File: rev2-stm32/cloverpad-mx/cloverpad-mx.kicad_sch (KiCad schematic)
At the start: 31 parts, among them J1 USB_C_Receptacle_USB2.0_16P, J2 Conn_01x04, SW1 SW_SPST, SW2 SW_SPST, U1 STM32F072CBT6, U2 XC6206PxxxMR, Y1 16MHz

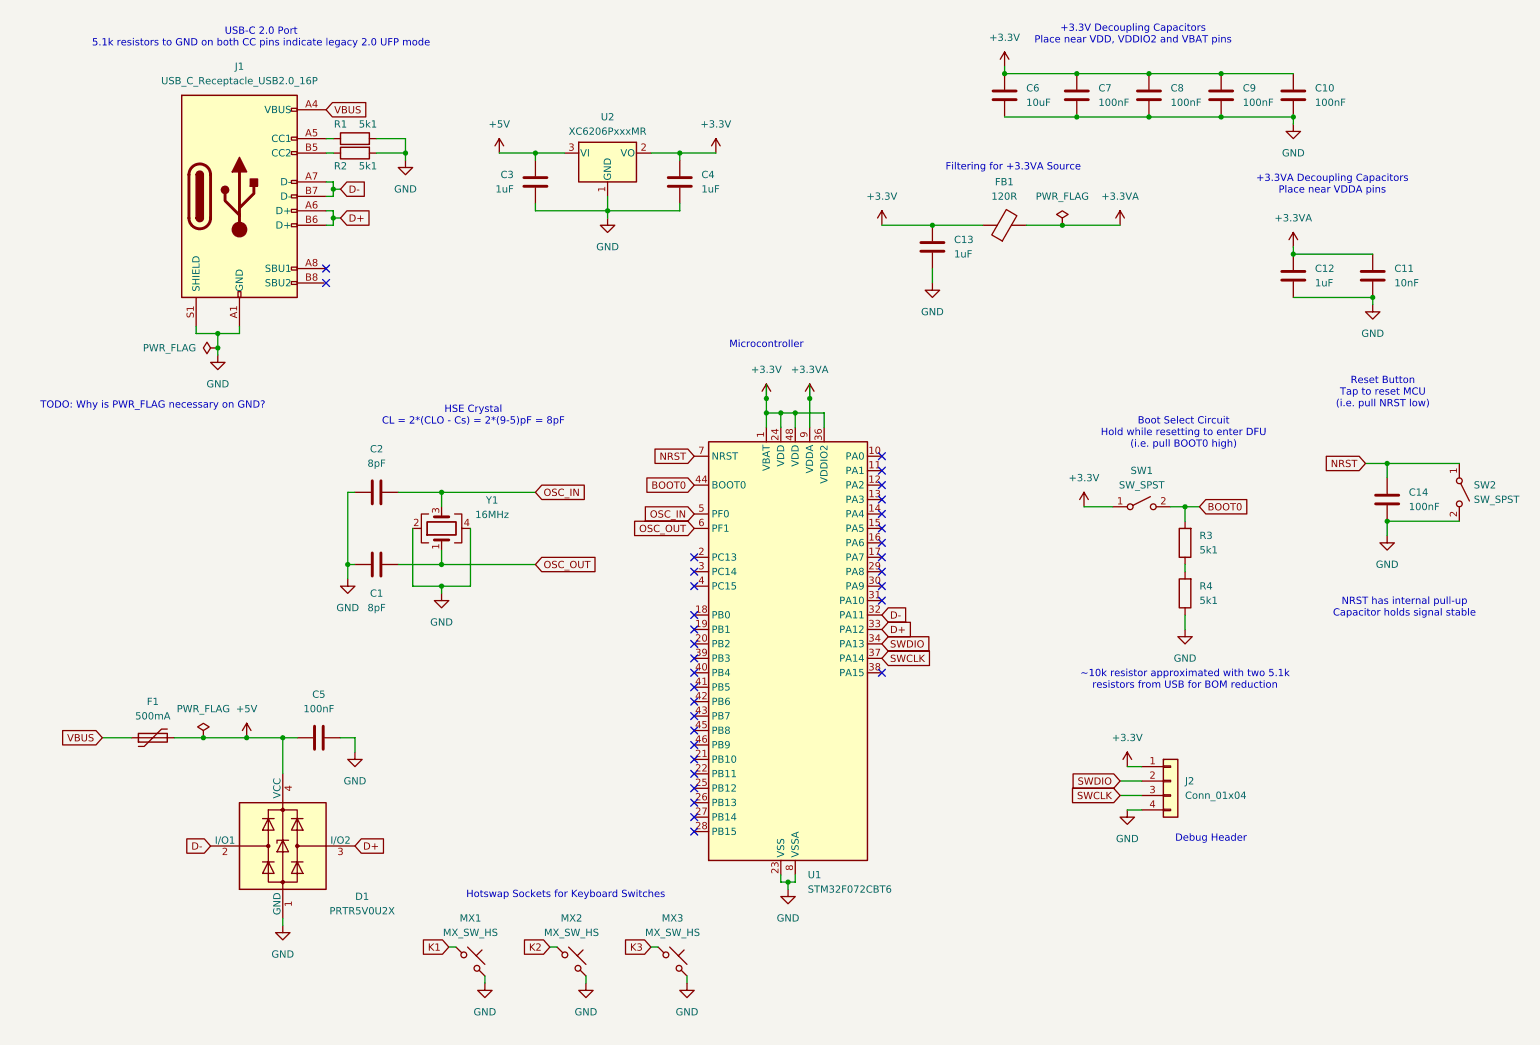
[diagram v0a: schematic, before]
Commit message: refactor: tidy up rev2-stm32 schematic
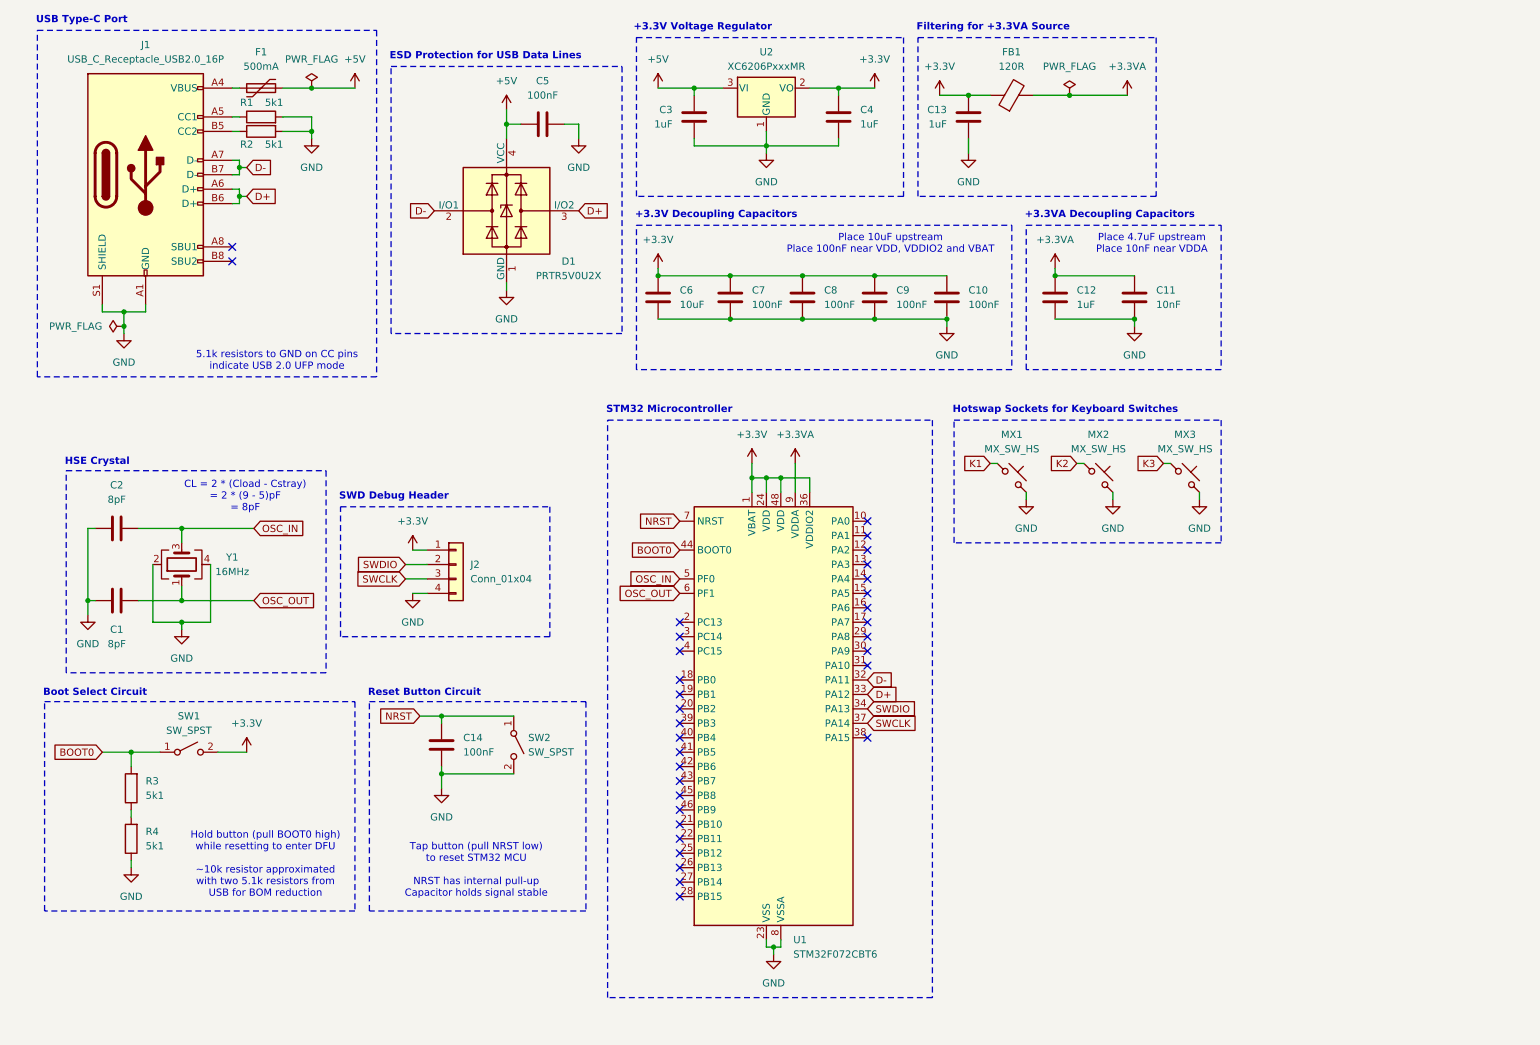
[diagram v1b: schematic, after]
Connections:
- net +3.3V: now also SW1.2 (B); no longer SW1.1 (A)
- net BOOT0: now also SW1.1 (A); no longer SW1.2 (B)
- net VBUS: no longer names the net of F1.1, J1.A4 (VBUS), J1.A9 (VBUS), J1.B4 (VBUS), J1.B9 (VBUS)
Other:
- note added: "+3.3V Decoupling Capacitors"
- note added: "+3.3V Voltage Regulator"
- note added: "+3.3VA Decoupling Capacitors"
- note added: "5.1k resistors to GND on CC pins indicate USB 2.0 UFP mode"
- note added: "Boot Select Circuit"
- note added: "CL = 2 * (Cload - Cstray) = 2 * (9 - 5)pF = 8pF"
- note added: "ESD Protection for USB Data Lines"
- note added: "HSE Crystal"
- note added: "Hold button (pull BOOT0 high) while resetting to enter DFU ~10k resistor approximated with two 5.1k resistors from USB for BOM reduction"
- note added: "Place 10uF upstream Place 100nF near VDD, VDDIO2 and VBAT"
- note added: "Place 4.7uF upstream Place 10nF near VDDA"
- note added: "Reset Button Circuit"
- note added: "STM32 Microcontroller"
- note added: "SWD Debug Header"
- note added: "Tap button (pull NRST low) to reset STM32 MCU NRST has internal pull-up Capacitor holds signal stable"
- note added: "USB Type-C Port"
- note removed: "+3.3V Decoupling Capacitors Place near VDD, VDDIO2 and VBAT pins"
- note removed: "+3.3VA Decoupling Capacitors Place near VDDA pins"
- note removed: "Boot Select Circuit Hold while resetting to enter DFU (i.e. pull BOOT0 high)"
- note removed: "Debug Header"
- note removed: "HSE Crystal CL = 2*(CLO - Cs) = 2*(9-5)pF = 8pF"
- note removed: "Microcontroller"
- note removed: "NRST has internal pull-up Capacitor holds signal stable"
- note removed: "Reset Button Tap to reset MCU (i.e. pull NRST low)"
- note removed: "TODO: Why is PWR_FLAG necessary on GND?"
- note removed: "USB-C 2.0 Port 5.1k resistors to GND on both CC pins indicate legacy 2.0 UFP mode"
- note removed: "~10k resistor approximated with two 5.1k resistors from USB for BOM reduction"
- moved on the sheet: C1, C10, C11, C12, C13, C14, C2, C3, C4, C5, C6, C7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

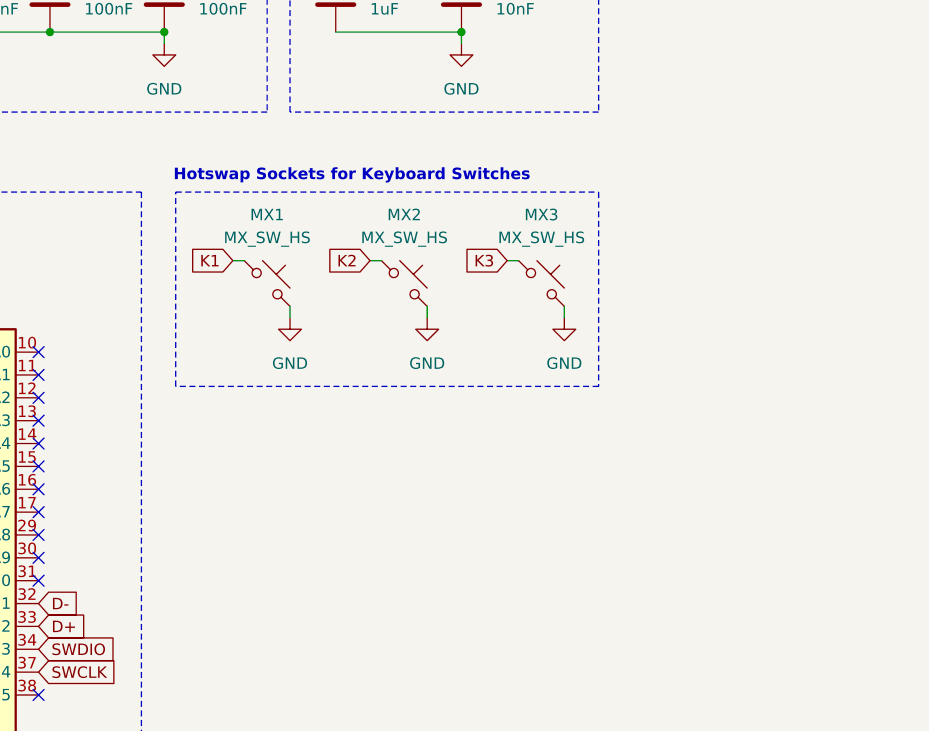
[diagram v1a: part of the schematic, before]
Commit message: feat: add m2 mounting holes to rev2-stm32 PCB
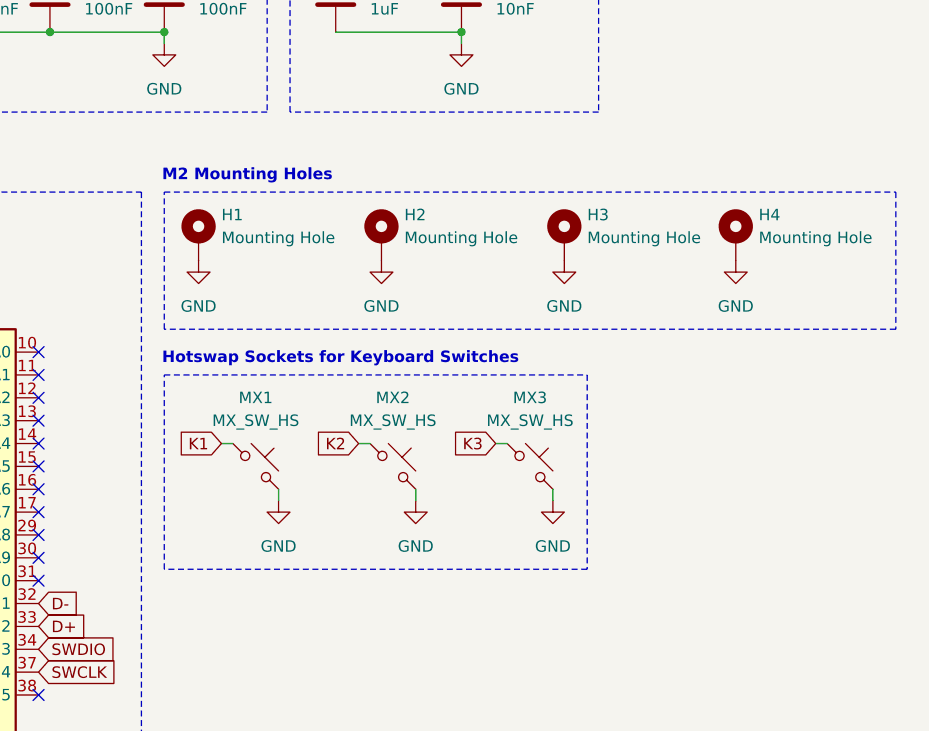
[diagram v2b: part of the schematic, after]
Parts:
- added H1, H2, H3, H4: Mounting Hole, MountingHole:MountingHole_2.2mm_M2_Pad, symbol Mechanical:MountingHole_Pad
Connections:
- net GND: now also H1.1, H2.1, H3.1, H4.1
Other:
- note added: "M2 Mounting Holes"
- moved on the sheet: MX1, MX2, MX3

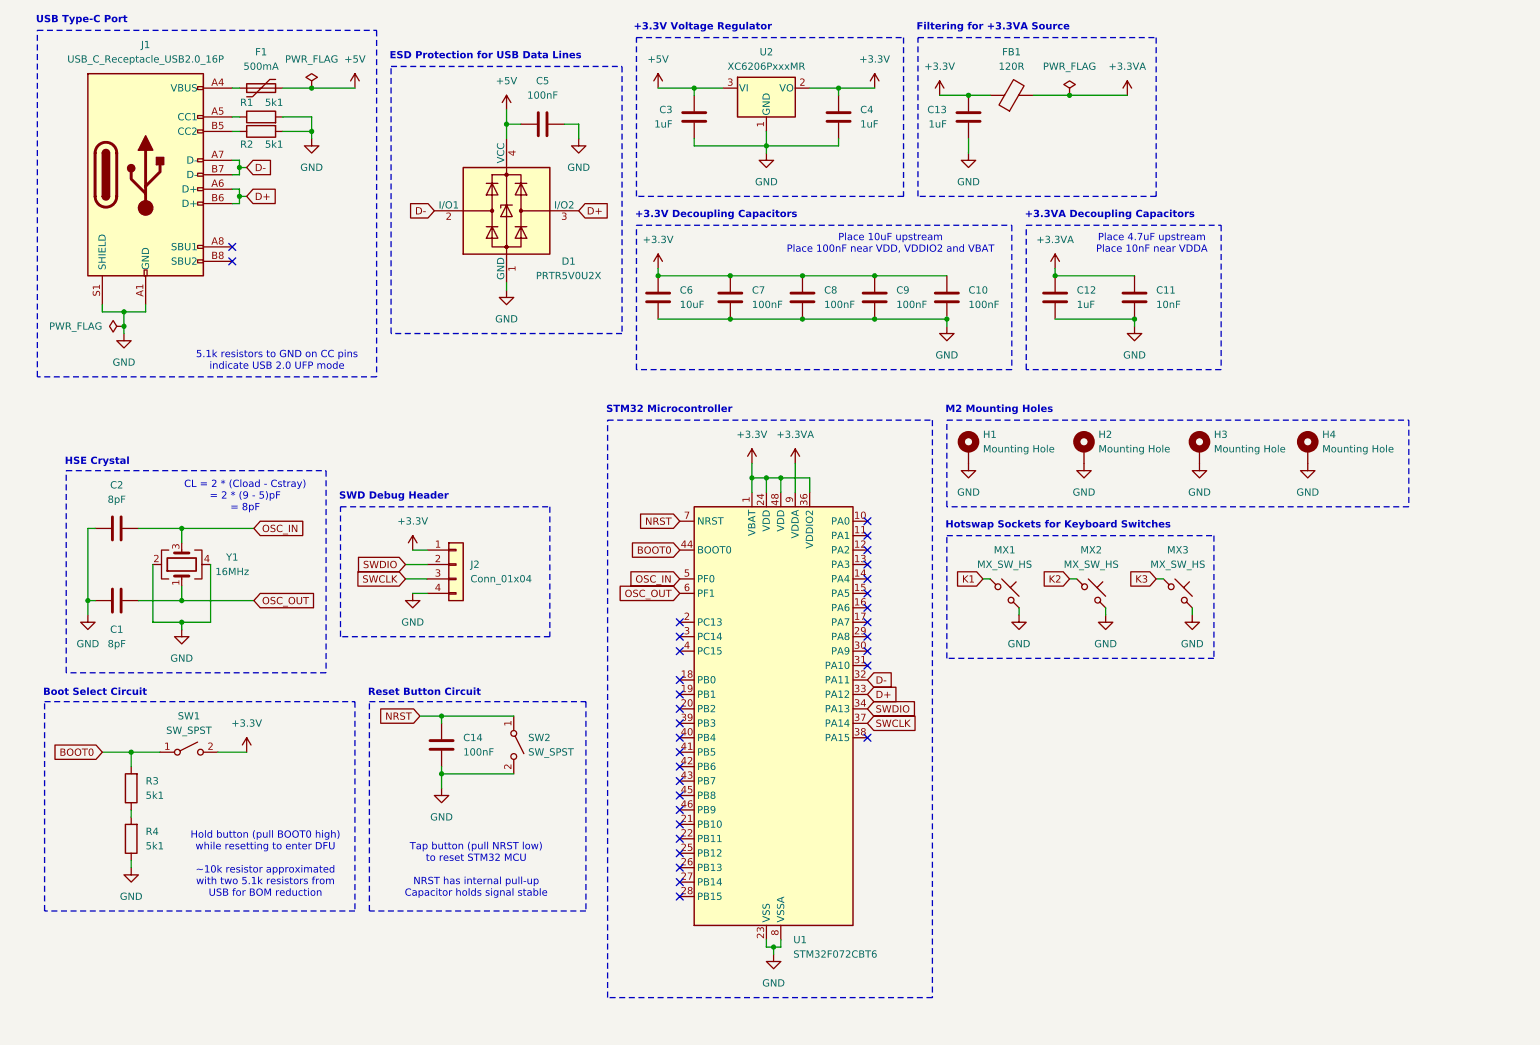
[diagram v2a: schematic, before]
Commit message: refactor: re-annotate components on rev2-stm32 PCB
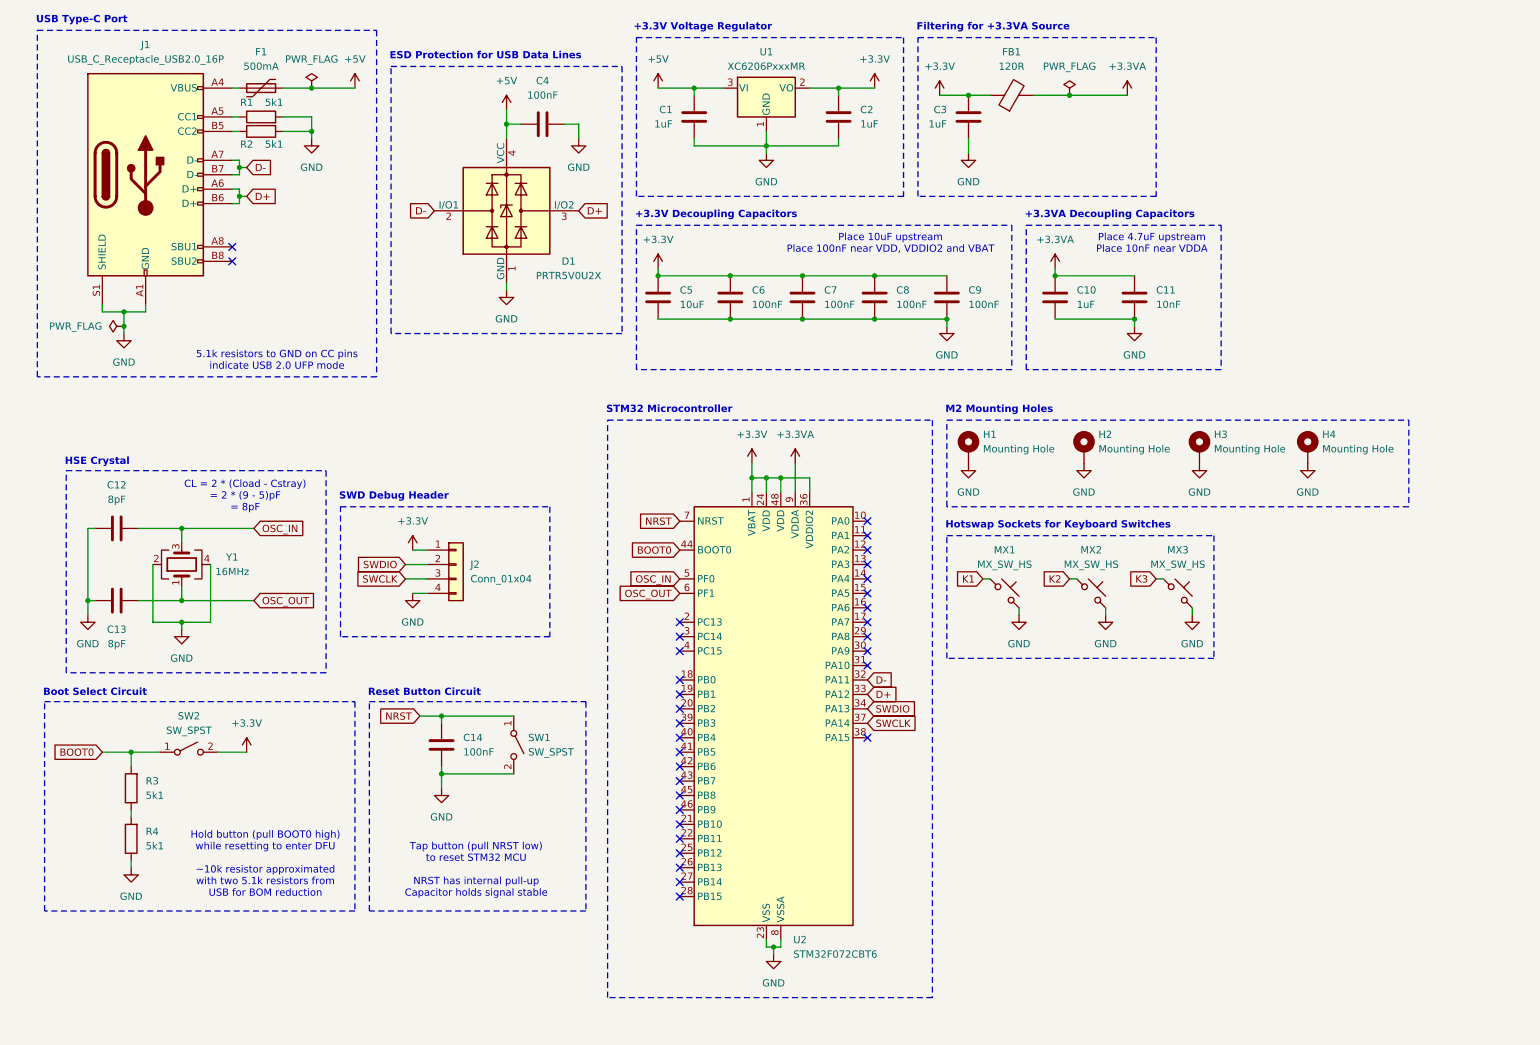
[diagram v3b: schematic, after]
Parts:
- renumbered C3 to C1, C12 to C10, C2 to C12, C1 to C13, C4 to C2, C13 to C3, C5 to C4, C6 to C5, C7 to C6, C8 to C7, C9 to C8, C10 to C9, SW2 to SW1, SW1 to SW2, U2 to U1, U1 to U2

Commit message: refactor: swap f072 with f401 has higher performance and on JLC, it doesn't cost much more. will need this for the ADC functionality later
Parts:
- removed U2: STM32F072CBT6, Package_QFP:LQFP-48_7x7mm_P0.5mm, symbol MCU_ST_STM32F0:STM32F072CBTx
- added C10: 100nF, Capacitor_SMD:C_0402_1005Metric, symbol Device:C
- added C16: 2.2uF, Capacitor_SMD:C_0603_1608Metric, symbol Device:C
- added U2: STM32F401RCTx, Package_QFP:LQFP-64_10x10mm_P0.5mm, symbol MCU_ST_STM32F4:STM32F401RCTx
- renumbered C10 to C11, C11 to C12, C12 to C13, C13 to C14, C14 to C15
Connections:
- net +3.3V: now also C10.1, U2.1 (VBAT), U2.19 (VDD), U2.32 (VDD), U2.48 (VDD), U2.64 (VDD)
- net +3.3VA: now also U2.13 (VREF+)
- net BOOT0: now also U2.60 (BOOT0)
- net D+: now also U2.45 (PA12)
- net D-: now also U2.44 (PA11)
- net GND: now also C10.2, C16.2, U2.12 (VSSA), U2.18 (VSS), U2.31 (VSS), U2.47 (VSS), U2.63 (VSS)
- net NRST: now also U2.7 (NRST)
- net OSC_IN: now also U2.5 (PH0)
- net OSC_OUT: now also U2.6 (PH1)
- net SWCLK: now also U2.49 (PA14)
- net SWDIO: now also U2.46 (PA13)
- new net: C16.1, U2.30 (VCAP1)
- no-connect marks 33 -> 46
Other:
- note added: "Place 10uF upstream Place 100nF near VDD and VBAT"
- note added: "VCAP1 is for internal 1.2V voltage regulator ESR must be < 2R"
- note removed: "Place 10uF upstream Place 100nF near VDD, VDDIO2 and VBAT"
- moved on the sheet: C11, C12, H1, H2, H3, H4, MX1, MX2, MX3
